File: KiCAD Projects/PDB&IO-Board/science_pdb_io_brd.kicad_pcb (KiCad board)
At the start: 2 copper layers, 2 parts, among them P3 BBB_P9_HEADER, P4 BBB_P8_HEADER

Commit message: Worked on PCB
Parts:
- added P5: CONN_01X06, Pin_Headers:Pin_Header_Straight_1x06_Pitch2.54mm, F.Cu at (94.6, 104.8)
- added P6: CONN_01X07, Pin_Headers:Pin_Header_Straight_1x07_Pitch2.54mm, F.Cu at (45.1, 102.9)
- added P7: CONN_01X05, Pin_Headers:Pin_Header_Straight_1x05_Pitch2.54mm, F.Cu at (68.6, 102.9)
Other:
- board text added: "Distance VL53L0X"
- board text added: "ETH Jack"
- board text added: "Thermocouple MAX31855"
- board text added: "UV Light VEML6070"
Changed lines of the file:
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@@
 (kicad_pcb (version 4) (host pcbnew 4.0.3-stable)
   (general
-    (links 7)
-    (no_connects 7)
-    (area 156.264762 87.44 213.940239 153.96)
+    (links 19)
+    (no_connects 19)
+    (area 0 0 0 0)
     (thickness 1.6)
-    (drawings 0)
+    (drawings 4)
     (tracks 0)
     (zones 0)
-    (modules 2)
-    (nets 86)
+    (modules 5)
+    (nets 92)
   )
   (page A4)
@@
   (net 84 MOTOR3_PWM)
   (net 85 MOTOR4_PWM)
+  (net 86 +5V)
+  (net 87 "Net-(P5-Pad2)")
+  (net 88 "Net-(P6-Pad1)")
+  (net 89 "Net-(P6-Pad6)")
+  (net 90 "Net-(P6-Pad7)")
+  (net 91 "Net-(P7-Pad5)")
   (net_class Default "This is the default net class."
     (clearance 0.2)
@@
     (uvia_dia 0.3)
     (uvia_drill 0.1)
+    (add_net +5V)
     (add_net GND)
     (add_net GNDA)
@@
     (add_net "Net-(P4-Pad7)")
     (add_net "Net-(P4-Pad9)")
+    (add_net "Net-(P5-Pad2)")
+    (add_net "Net-(P6-Pad1)")
+    (add_net "Net-(P6-Pad6)")
+    (add_net "Net-(P6-Pad7)")
+    (add_net "Net-(P7-Pad5)")
     (add_net SPI_CLK)
     (add_net SPI_CS)
@@
     )
   )
+  (module Pin_Headers:Pin_Header_Straight_1x06_Pitch2.54mm (layer F.Cu)
+    (at 94.615 104.775)
+    (descr "Through hole straight pin header, 1x06, 2.54mm pitch, single row")
+    (tags "Through hole pin header THT 1x06 2.54mm single row")
+    (fp_text reference P5 (at 0 -2.39) (layer F.SilkS)
+      (effects (font (size 1 1) (thickness 0.15)))
+    )
+    (fp_text value CONN_01X06 (at 0 15.09) (layer F.Fab) hide
+      (effects (font (size 1 1) (thickness 0.15)))
+    )
+    (fp_line (start -1.27 -1.27) (end -1.27 13.97) (layer F.Fab) (width 0.1))
+    (fp_line (start -1.27 13.97) (end 1.27 13.97) (layer F.Fab) (width 0.1))
+    (fp_line (start 1.27 13.97) (end 1.27 -1.27) (layer F.Fab) (width 0.1))
+    (fp_line (start 1.27 -1.27) (end -1.27 -1.27) (layer F.Fab) (width 0.1))
+    (fp_line (start -1.39 1.27) (end -1.39 14.09) (layer F.SilkS) (width 0.12))
+    (fp_line (start -1.39 14.09) (end 1.39 14.09) (layer F.SilkS) (width 0.12))
+    (fp_line (start 1.39 14.09) (end 1.39 1.27) (layer F.SilkS) (width 0.12))
+    (fp_line (start 1.39 1.27) (end -1.39 1.27) (layer F.SilkS) (width 0.12))
+    (fp_line (start -1.39 0) (end -1.39 -1.39) (layer F.SilkS) (width 0.12))
+    (fp_line (start -1.39 -1.39) (end 0 -1.39) (layer F.SilkS) (width 0.12))
+    (fp_line (start -1.6 -1.6) (end -1.6 14.3) (layer F.CrtYd) (width 0.05))
+    (fp_line (start -1.6 14.3) (end 1.6 14.3) (layer F.CrtYd) (width 0.05))
+    (fp_line (start 1.6 14.3) (end 1.6 -1.6) (layer F.CrtYd) (width 0.05))
+    (fp_line (start 1.6 -1.6) (end -1.6 -1.6) (layer F.CrtYd) (width 0.05))
+    (pad 1 thru_hole rect (at 0 0) (size 1.7 1.7) (drill 1) (layers *.Cu *.Mask)
+      (net 86 +5V))
+    (pad 2 thru_hole oval (at 0 2.54) (size 1.7 1.7) (drill 1) (layers *.Cu *.Mask)
+      (net 87 "Net-(P5-Pad2)"))
+    (pad 3 thru_hole oval (at 0 5.08) (size 1.7 1.7) (drill 1) (layers *.Cu *.Mask)
+      (net 1 GND))
+    (pad 4 thru_hole oval (at 0 7.62) (size 1.7 1.7) (drill 1) (layers *.Cu *.Mask)
+      (net 20 SPI_DO))
+    (pad 5 thru_hole oval (at 0 10.16) (size 1.7 1.7) (drill 1) (layers *.Cu *.Mask)
+      (net 16 SPI_CS))
+    (pad 6 thru_hole oval (at 0 12.7) (size 1.7 1.7) (drill 1) (layers *.Cu *.Mask)
+      (net 21 SPI_CLK))
+    (model Pin_Headers.3dshapes/Pin_Header_Straight_1x06_Pitch2.54mm.wrl
+      (at (xyz 0 -0.25 0))
+      (scale (xyz 1 1 1))
+      (rotate (xyz 0 0 90))
+    )
+  )
+  (module Pin_Headers:Pin_Header_Straight_1x07_Pitch2.54mm (layer F.Cu)
+    (at 45.085 102.87)
+    (descr "Through hole straight pin header, 1x07, 2.54mm pitch, single row")
+    (tags "Through hole pin header THT 1x07 2.54mm single row")
+    (fp_text reference P6 (at 0 -2.39) (layer F.SilkS)
+      (effects (font (size 1 1) (thickness 0.15)))
+    )
+    (fp_text value CONN_01X07 (at 0 17.63) (layer F.Fab) hide
+      (effects (font (size 1 1) (thickness 0.15)))
+    )
+    (fp_line (start -1.27 -1.27) (end -1.27 16.51) (layer F.Fab) (width 0.1))
+    (fp_line (start -1.27 16.51) (end 1.27 16.51) (layer F.Fab) (width 0.1))
+    (fp_line (start 1.27 16.51) (end 1.27 -1.27) (layer F.Fab) (width 0.1))
+    (fp_line (start 1.27 -1.27) (end -1.27 -1.27) (layer F.Fab) (width 0.1))
+    (fp_line (start -1.39 1.27) (end -1.39 16.63) (layer F.SilkS) (width 0.12))
+    (fp_line (start -1.39 16.63) (end 1.39 16.63) (layer F.SilkS) (width 0.12))
+    (fp_line (start 1.39 16.63) (end 1.39 1.27) (layer F.SilkS) (width 0.12))
+    (fp_line (start 1.39 1.27) (end -1.39 1.27) (layer F.SilkS) (width 0.12))
+    (fp_line (start -1.39 0) (end -1.39 -1.39) (layer F.SilkS) (width 0.12))
+    (fp_line (start -1.39 -1.39) (end 0 -1.39) (layer F.SilkS) (width 0.12))
+    (fp_line (start -1.6 -1.6) (end -1.6 16.8) (layer F.CrtYd) (width 0.05))
+    (fp_line (start -1.6 16.8) (end 1.6 16.8) (layer F.CrtYd) (width 0.05))
+    (fp_line (start 1.6 16.8) (end 1.6 -1.6) (layer F.CrtYd) (width 0.05))
+    (fp_line (start 1.6 -1.6) (end -1.6 -1.6) (layer F.CrtYd) (width 0.05))
+    (pad 1 thru_hole rect (at 0 0) (size 1.7 1.7) (drill 1) (layers *.Cu *.Mask)
+      (net 88 "Net-(P6-Pad1)"))
+    (pad 2 thru_hole oval (at 0 2.54) (size 1.7 1.7) (drill 1) (layers *.Cu *.Mask)
+      (net 86 +5V))
+    (pad 3 thru_hole oval (at 0 5.08) (size 1.7 1.7) (drill 1) (layers *.Cu *.Mask)
+      (net 1 GND))
+    (pad 4 thru_hole oval (at 0 7.62) (size 1.7 1.7) (drill 1) (layers *.Cu *.Mask)
+      (net 19 I2C_SDA))
+    (pad 5 thru_hole oval (at 0 10.16) (size 1.7 1.7) (drill 1) (layers *.Cu *.Mask)
+      (net 18 I2C_SCL))
+    (pad 6 thru_hole oval (at 0 12.7) (size 1.7 1.7) (drill 1) (layers *.Cu *.Mask)
+      (net 89 "Net-(P6-Pad6)"))
+    (pad 7 thru_hole oval (at 0 15.24) (size 1.7 1.7) (drill 1) (layers *.Cu *.Mask)
+      (net 90 "Net-(P6-Pad7)"))
+    (model Pin_Headers.3dshapes/Pin_Header_Straight_1x07_Pitch2.54mm.wrl
+      (at (xyz 0 -0.3 0))
+      (scale (xyz 1 1 1))
+      (rotate (xyz 0 0 90))
+    )
+  )
+  (module Pin_Headers:Pin_Header_Straight_1x05_Pitch2.54mm (layer F.Cu)
+    (at 68.58 102.87)
+    (descr "Through hole straight pin header, 1x05, 2.54mm pitch, single row")
+    (tags "Through hole pin header THT 1x05 2.54mm single row")
+    (fp_text reference P7 (at 0 -2.39) (layer F.SilkS)
+      (effects (font (size 1 1) (thickness 0.15)))
+    )
+    (fp_text value CONN_01X05 (at 0 12.55) (layer F.Fab) hide
+      (effects (font (size 1 1) (thickness 0.15)))
+    )
+    (fp_line (start -1.27 -1.27) (end -1.27 11.43) (layer F.Fab) (width 0.1))
+    (fp_line (start -1.27 11.43) (end 1.27 11.43) (layer F.Fab) (width 0.1))
+    (fp_line (start 1.27 11.43) (end 1.27 -1.27) (layer F.Fab) (width 0.1))
+    (fp_line (start 1.27 -1.27) (end -1.27 -1.27) (layer F.Fab) (width 0.1))
+    (fp_line (start -1.39 1.27) (end -1.39 11.55) (layer F.SilkS) (width 0.12))
+    (fp_line (start -1.39 11.55) (end 1.39 11.55) (layer F.SilkS) (width 0.12))
+    (fp_line (start 1.39 11.55) (end 1.39 1.27) (layer F.SilkS) (width 0.12))
+    (fp_line (start 1.39 1.27) (end -1.39 1.27) (layer F.SilkS) (width 0.12))
+    (fp_line (start -1.39 0) (end -1.39 -1.39) (layer F.SilkS) (width 0.12))
+    (fp_line (start -1.39 -1.39) (end 0 -1.39) (layer F.SilkS) (width 0.12))
+    (fp_line (start -1.6 -1.6) (end -1.6 11.7) (layer F.CrtYd) (width 0.05))
+    (fp_line (start -1.6 11.7) (end 1.6 11.7) (layer F.CrtYd) (width 0.05))
+    (fp_line (start 1.6 11.7) (end 1.6 -1.6) (layer F.CrtYd) (width 0.05))
+    (fp_line (start 1.6 -1.6) (end -1.6 -1.6) (layer F.CrtYd) (width 0.05))
+    (pad 1 thru_hole rect (at 0 0) (size 1.7 1.7) (drill 1) (layers *.Cu *.Mask)
+      (net 86 +5V))
+    (pad 2 thru_hole oval (at 0 2.54) (size 1.7 1.7) (drill 1) (layers *.Cu *.Mask)
+      (net 1 GND))
+    (pad 3 thru_hole oval (at 0 5.08) (size 1.7 1.7) (drill 1) (layers *.Cu *.Mask)
+      (net 18 I2C_SCL))
+    (pad 4 thru_hole oval (at 0 7.62) (size 1.7 1.7) (drill 1) (layers *.Cu *.Mask)
+      (net 19 I2C_SDA))
+    (pad 5 thru_hole oval (at 0 10.16) (size 1.7 1.7) (drill 1) (layers *.Cu *.Mask)
+      (net 91 "Net-(P7-Pad5)"))
+    (model Pin_Headers.3dshapes/Pin_Header_Straight_1x05_Pitch2.54mm.wrl
+      (at (xyz 0 -0.2 0))
+      (scale (xyz 1 1 1))
+      (rotate (xyz 0 0 90))
+    )
+  )
+  (gr_text "Distance\nVL53L0X" (at 40.64 110.49 90) (layer F.Cu)
+    (effects (font (size 1.5 1.5) (thickness 0.3)))
+  )
+  (gr_text "UV Light\nVEML6070" (at 64.135 107.95 90) (layer F.Cu)
+    (effects (font (size 1.5 1.5) (thickness 0.3)))
+  )
+  (gr_text "Thermocouple\nMAX31855" (at 90.17 111.125 90) (layer F.Cu)
+    (effects (font (size 1.5 1.5) (thickness 0.3)))
+  )
+  (gr_text "ETH\nJack" (at 76.835 20.32) (layer F.Cu)
+    (effects (font (size 1.5 1.5) (thickness 0.3)))
+  )
 )

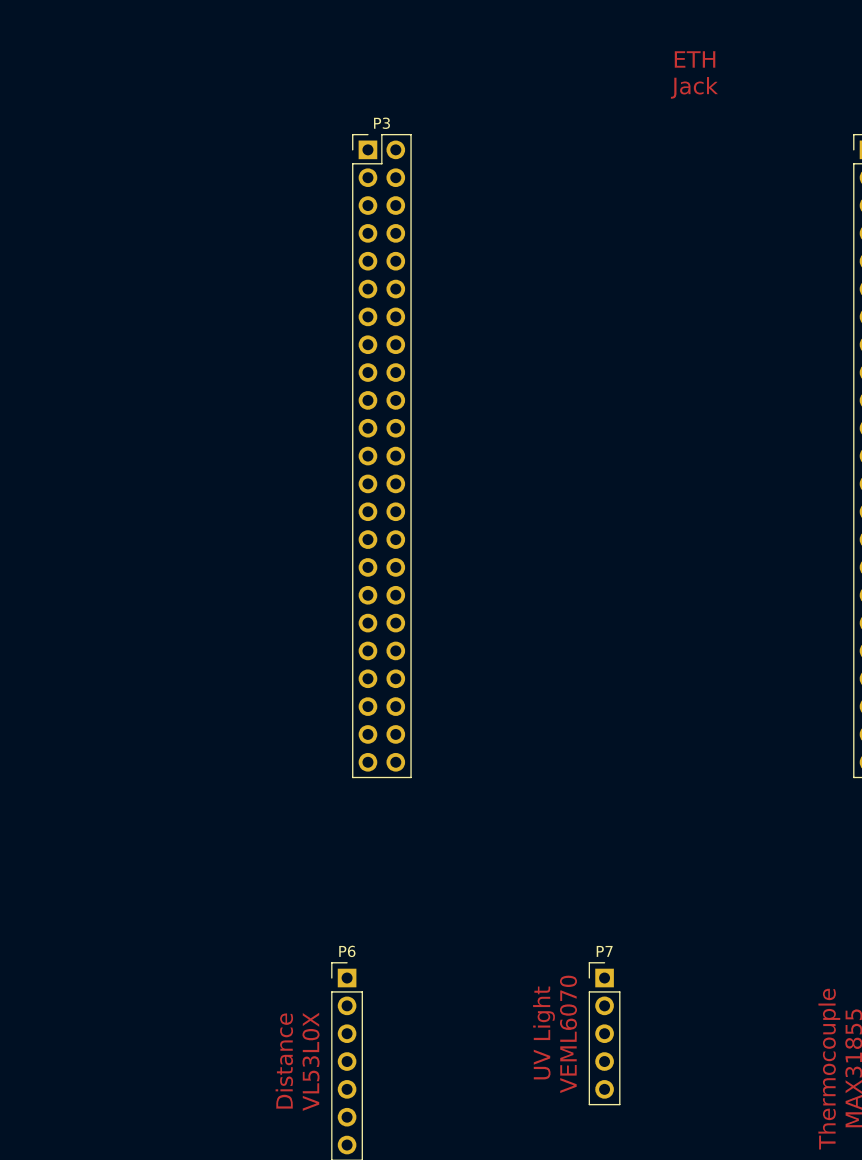
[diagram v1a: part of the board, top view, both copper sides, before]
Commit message: Created Power Distribution Board. Moved stuff to it.
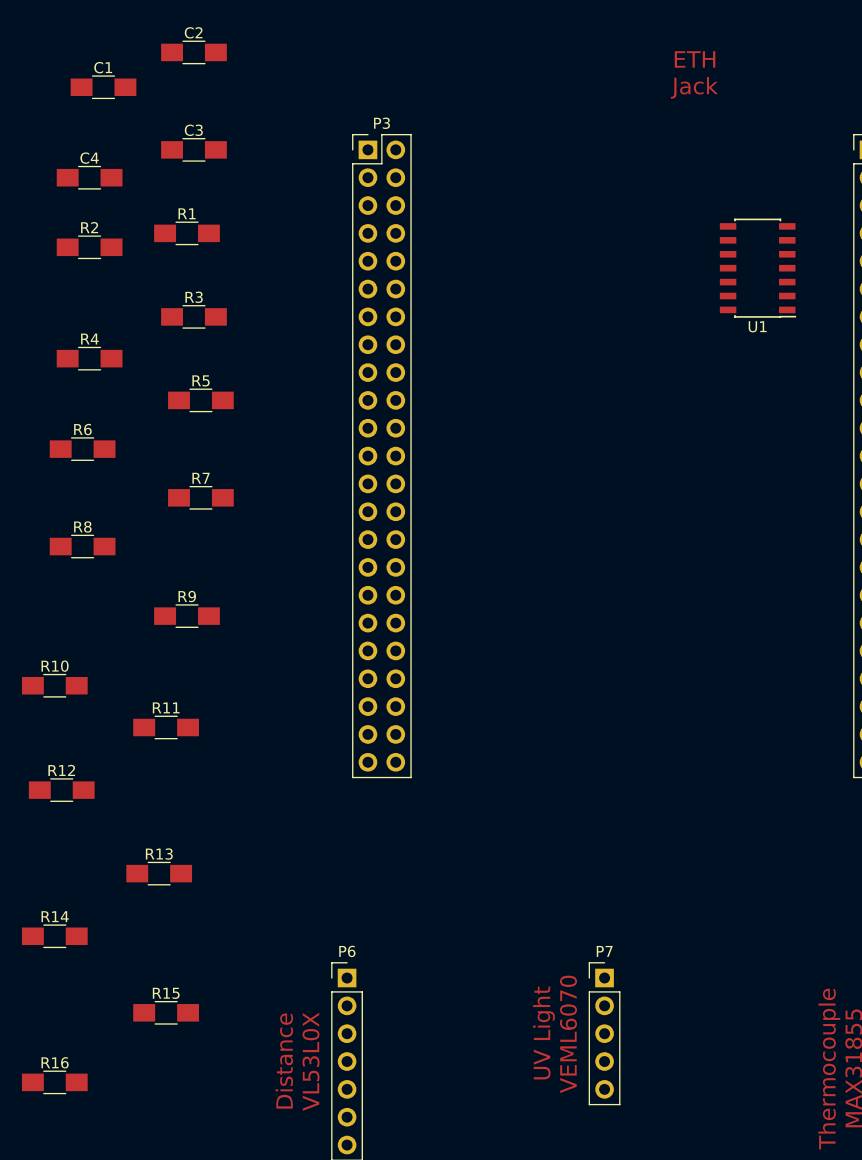
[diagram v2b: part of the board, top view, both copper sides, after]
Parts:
- added C1: 1u, Capacitors_SMD:C_1206_HandSoldering, F.Cu at (22.9, 21.6)
- added C2: 1u, Capacitors_SMD:C_1206_HandSoldering, F.Cu at (31.1, 18.4)
- added C3: 1u, Capacitors_SMD:C_1206_HandSoldering, F.Cu at (31.1, 27.3)
- added C4: C, Capacitors_SMD:C_1206_HandSoldering, F.Cu at (21.6, 29.8)
- added R1: 1k, Capacitors_SMD:C_1206_HandSoldering, F.Cu at (30.5, 34.9)
- added R10: 5k, Capacitors_SMD:C_1206_HandSoldering, F.Cu at (18.4, 76.2)
- added R11: 5k, Capacitors_SMD:C_1206_HandSoldering, F.Cu at (28.6, 80.0)
- added R12: 5k, Capacitors_SMD:C_1206_HandSoldering, F.Cu at (19.1, 85.7)
- added R13: 5k, Capacitors_SMD:C_1206_HandSoldering, F.Cu at (27.9, 93.3)
- added R14: 5k, Capacitors_SMD:C_1206_HandSoldering, F.Cu at (18.4, 99.1)
- added R15: R, Capacitors_SMD:C_1206_HandSoldering, F.Cu at (28.6, 106.0)
- added R16: R, Capacitors_SMD:C_1206_HandSoldering, F.Cu at (18.4, 112.4)
- added R2: 560, Capacitors_SMD:C_1206_HandSoldering, F.Cu at (21.6, 36.2)
- added R3: 5k, Capacitors_SMD:C_1206_HandSoldering, F.Cu at (31.1, 42.5)
- added R4: 5k, Capacitors_SMD:C_1206_HandSoldering, F.Cu at (21.6, 46.4)
- added R5: 5k, Capacitors_SMD:C_1206_HandSoldering, F.Cu at (31.8, 50.2)
- added R6: 5k, Capacitors_SMD:C_1206_HandSoldering, F.Cu at (21.0, 54.6)
- added R7: 5k, Capacitors_SMD:C_1206_HandSoldering, F.Cu at (31.8, 59.1)
- added R8: 5k, Capacitors_SMD:C_1206_HandSoldering, F.Cu at (21.0, 63.5)
- added R9: 5k, Capacitors_SMD:C_1206_HandSoldering, F.Cu at (30.5, 69.8)
- added U1: SN74HC14N, Housings_SOIC:SOIC-14_3.9x8.7mm_Pitch1.27mm, F.Cu at (82.5, 38.1)
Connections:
- P4 pad 12: LIMIT3_IN -> LIMIT1_IN
- P4 pad 8: LIMIT1_IN -> LIMIT3_IN

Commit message: Worked on Main Board
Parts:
- removed R15: R, Capacitors_SMD:C_1206_HandSoldering
- added P2: RPI_HEADER, Pin_Headers:Pin_Header_Straight_2x20_Pitch2.54mm, F.Cu at (142.2, 39.4)
- added R17: 80Ω, Capacitors_SMD:C_1206_HandSoldering, F.Cu at (17.8, 116.8)
- C1, C2, C3: value 1u -> 1μF
- P5: value CONN_01X06 -> THERMO_SENS
- P6: value CONN_01X07 -> DIST_SENS
- P7: value CONN_01X05 -> UV_SENS
- R1: value 1k -> 1kΩ
- R10, R11, R12, R13, R14, R3, R4, R5, R6, R7, R8, R9: value 5k -> 5kΩ
- R16: value R -> 180Ω
- R2: value 560 -> 560Ω
- U1: moved to B.Cu
- moved R14 114.8 mm to (123.2, 52.1), turned to 180 degrees
- moved R12 110.7 mm to (123.2, 48.3), turned to 180 degrees
- moved R13 102.4 mm to (123.2, 55.9), turned to 180 degrees
- moved R6 88.5 mm to (108.0, 71.1), turned to 180 degrees
- moved R10 87.7 mm to (105.4, 64.8), turned to 180 degrees
- moved R8 87.7 mm to (108.0, 74.9), turned to 180 degrees
- moved C4 87.1 mm to (106.7, 48.3)
- moved R11 79.2 mm to (105.4, 61.0), turned to 180 degrees
- moved R7 78.7 mm to (108.0, 78.7), turned to 180 degrees
- moved R9 76.0 mm to (105.4, 57.1), turned to 180 degrees
- moved R4 28.7 mm to (38.1, 22.9)
- moved C1 27.5 mm to (38.1, 44.5)
- moved C3 26.0 mm to (31.8, 53.3)
- moved U1 24.1 mm to (106.7, 38.1), turned to 0 degrees
- moved C2 10.8 mm to (38.1, 26.7)
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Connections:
- net B_LIM1 renamed /B_LIM1
- net B_LIM2 renamed /B_LIM2
- net B_LIM3 renamed /B_LIM3
- net GND renamed GNDD
- net I2C_SCL renamed /I2C_SCL
- net I2C_SDA renamed /I2C_SDA
- net LIMIT1_IN renamed /LIMIT1_IN
- net LIMIT2_IN renamed /LIMIT2_IN
- net LIMIT3_IN renamed /LIMIT3_IN
- net MOISTURE_IN renamed /MOISTURE_IN
- net MOTOR1_PWM renamed /MOTOR1_PWM
- net MOTOR2_PWM renamed /MOTOR2_PWM
- net MOTOR3_PWM renamed /MOTOR3_PWM
- net MOTOR4_PWM renamed /MOTOR4_PWM
- net SPI_CLK renamed /SPI_CLK
- net SPI_CS renamed /SPI_CS
- net SPI_DI renamed /SPI_DI
- net SPI_DO renamed /SPI_DO
- C4 pad 1: +5V -> +3V3
- P3 pad 15: Net-(P3-Pad15) -> /CAM_TRIG
- P3 pad 3: Net-(P3-Pad3) -> +3V3
- P3 pad 4: Net-(P3-Pad4) -> +3V3
- P3 pad 5: Net-(P3-Pad5) -> +5V
- P3 pad 6: Net-(P3-Pad6) -> +5V
- P4 pad 20: Net-(P4-Pad20) -> /ENC1_BUT
- P4 pad 22: Net-(P4-Pad22) -> /ENC1_A
- P4 pad 24: Net-(P4-Pad24) -> /ENC1_B
- P4 pad 26: Net-(P4-Pad26) -> /ENC2_BUT
- P4 pad 28: Net-(P4-Pad28) -> /ENC2_A
- P4 pad 30: Net-(P4-Pad30) -> /ENC2_B
- P4 pad 32: Net-(P4-Pad32) -> /ENC3_BUT
- P4 pad 34: Net-(P4-Pad34) -> /ENC3_A
- P4 pad 36: Net-(P4-Pad36) -> /ENC3_B
- P5 pad 1: +5V -> +3V3
- P6 pad 2: +5V -> +3V3
- P7 pad 1: +5V -> +3V3
- R10 pad 1: +5V -> +3V3
- R10 pad 2: ENC2_B -> /ENC2_B
- R11 pad 1: +5V -> +3V3
- R11 pad 2: ENC2_A -> /ENC2_A
- R12 pad 1: +5V -> +3V3
- R12 pad 2: ENC1_BUT -> /ENC1_BUT
- R13 pad 1: +5V -> +3V3
- R13 pad 2: ENC1_B -> /ENC1_B
- R14 pad 1: +5V -> +3V3
- R14 pad 2: ENC1_A -> /ENC1_A
- R3 pad 2: +5V -> +3V3
- R4 pad 2: +5V -> +3V3
- R5 pad 2: +5V -> +3V3
- R6 pad 1: +5V -> +3V3
- R6 pad 2: ENC3_BUT -> /ENC3_BUT
- R7 pad 1: +5V -> +3V3
- R7 pad 2: ENC3_B -> /ENC3_B
- R8 pad 1: +5V -> +3V3
- R8 pad 2: ENC3_A -> /ENC3_A
- R9 pad 1: +5V -> +3V3
- R9 pad 2: ENC2_BUT -> /ENC2_BUT
- U1 pad 14: +5V -> +3V3
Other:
- board outline added: 51.4 x 9.7 mm

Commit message: Progrss on Main Board Layout
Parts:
- added D2: LED, LEDs:LED_D5.0mm, F.Cu at (64.8, 47.0)
- added D3: LED, LEDs:LED_D5.0mm, F.Cu at (77.5, 47.0)
- added P11: ENCODER_1, Pin_Headers:Pin_Header_Straight_1x05_Pitch2.54mm, F.Cu at (102.9, 36.8)
- added P13: LIMIT1_IN, Pin_Headers:Pin_Header_Straight_1x03_Pitch2.54mm, F.Cu at (156.2, 43.2)
- added P14: LIMIT2_IN, Pin_Headers:Pin_Header_Straight_1x03_Pitch2.54mm, F.Cu at (161.3, 17.8)
- added P15: LIMIT3_IN, Pin_Headers:Pin_Header_Straight_1x03_Pitch2.54mm, F.Cu at (160.0, 33.0)
- added P16: ENCODER_3, Pin_Headers:Pin_Header_Straight_1x05_Pitch2.54mm, F.Cu at (102.9, 72.4)
- added P17: MOTOR1_PWM, Pin_Headers:Pin_Header_Straight_1x03_Pitch2.54mm, F.Cu at (78.7, 62.2)
- added P18: MOTOR2_PWM, Pin_Headers:Pin_Header_Straight_1x03_Pitch2.54mm, F.Cu at (78.7, 68.6)
- added P19: MOTOR3_PWM, Pin_Headers:Pin_Header_Straight_1x03_Pitch2.54mm, F.Cu at (78.7, 74.9)
- added P20: MOTOR4_PWM, Pin_Headers:Pin_Header_Straight_1x03_Pitch2.54mm, F.Cu at (78.7, 81.3)
- added P21: MOISTURE_CONN, Pin_Headers:Pin_Header_Straight_1x03_Pitch2.54mm, F.Cu at (62.9, 74.3)
- added P8: ENCODER_2, Pin_Headers:Pin_Header_Straight_1x05_Pitch2.54mm, F.Cu at (102.9, 54.6)
- moved C1 131.0 mm to (168.9, 38.1)
- moved C2 131.0 mm to (168.9, 20.3)
- moved C3 131.0 mm to (162.6, 47.0)
- moved R3 131.0 mm to (168.9, 34.3)
- moved R4 131.0 mm to (168.9, 16.5)
- moved R5 131.0 mm to (162.6, 43.8)
- moved P2 115.6 mm to (26.7, 40.6)
- moved R17 97.8 mm to (77.5, 39.4)
- moved R16 87.4 mm to (64.8, 39.4), turned to 180 degrees
- moved R2 48.0 mm to (55.9, 69.8), turned to 180 degrees
- moved R1 47.6 mm to (55.9, 73.7), turned to 180 degrees
- moved U1 29.5 mm to (133.3, 25.4)
- moved C4 29.5 mm to (133.3, 35.6)
- moved R13 19.8 mm to (109.2, 41.9)
- moved R14 19.8 mm to (109.2, 38.1)
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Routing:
- net /MOTOR1_PWM: track 0.00 -> 34.3 mm
- net /MOTOR2_PWM: track 0.00 -> 28.4 mm
- net /ENC3_BUT: track 0.00 -> 26.4 mm
- net /ENC1_A: track 0.00 -> 25.1 mm
- net /ENC1_B: track 0.00 -> 24.6 mm
- net /MOTOR4_PWM: track 0.00 -> 22.9 mm
- net /MOTOR3_PWM: track 0.00 -> 19.1 mm
- net /ENC3_A: track 0.00 -> 18.7 mm
- net /ENC3_B: track 0.00 -> 18.2 mm
- net /ENC1_BUT: track 0.00 -> 17.5 mm
- net GNDA: track 0.00 -> 16.5 mm
- net /ENC2_BUT: track 0.00 -> 16.2 mm
- net /ENC2_A: track 0.00 -> 14.9 mm
- net /ENC2_B: track 0.00 -> 13.3 mm
- net /MOISTURE_IN: track 0.00 -> 12.5 mm
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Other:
- net class Default: trace_width 0.25 -> 0.508

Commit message: Continued on Main PCB layout. Getting there.
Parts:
- C4, D2, D3, P11, P13, P14, P15, P16, P17, P18, P19, P20, P21, P5, P6, P7, P8: moved to B.Cu
- moved P2 103.5 mm to (104.8, 108.6), turned to 90 degrees
- moved R16 61.6 mm to (84.5, 97.8)
- moved R17 61.6 mm to (97.2, 97.8)
- moved D2 61.6 mm to (84.5, 105.4)
- moved D3 61.6 mm to (97.2, 105.4)
- moved R3 53.2 mm to (116.2, 27.3), turned to 90 degrees
- moved C1 50.1 mm to (120.0, 27.3), turned to 270 degrees
- moved P5 49.0 mm to (47.0, 105.4), turned to 0 degrees
- moved R4 45.1 mm to (125.1, 27.3), turned to 90 degrees
- moved C2 40.6 mm to (128.9, 27.3), turned to 270 degrees
- moved P15 38.1 mm to (121.9, 33.0), turned to 180 degrees
- moved P14 36.4 mm to (128.3, 33.0), turned to 180 degrees
- moved R5 33.0 mm to (134.0, 27.3), turned to 90 degrees
- moved C3 31.6 mm to (137.8, 27.3), turned to 270 degrees
- moved P13 23.9 mm to (134.6, 33.0), turned to 180 degrees
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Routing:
- net /I2C_SCL: track 0.00 -> 89.3 mm
- net /I2C_SDA: track 0.00 -> 65.3 mm
- net /SPI_CS: track 0.00 -> 52.5 mm
- net /B_LIM1: track 0.00 -> 52.5 mm
- net /SPI_DO: track 0.00 -> 51.2 mm
- net /SPI_CLK: track 0.00 -> 45.2 mm
- net /B_LIM2: track 0.00 -> 40.2 mm
- net /LIMIT3_IN: track 0.00 -> 27.8 mm
- net /LIMIT2_IN: track 0.00 -> 25.7 mm
- net /LIMIT1_IN: track 0.00 -> 23.5 mm
- net /B_LIM3: track 0.00 -> 22.9 mm
- net GNDD: track 0.00 -> 4.08 mm
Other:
- board size 51.4 x 9.7 mm -> 124 x 94.6 mm
- net class Default: via_dia 0.6 -> 0.762; via_drill 0.4 -> 0.508
